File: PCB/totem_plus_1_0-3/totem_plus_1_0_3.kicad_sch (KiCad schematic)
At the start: 92 parts, among them J1 MJ-4PP-9, J2 MJ-4PP-9, U1 xiao-ble, U2 xiao-ble

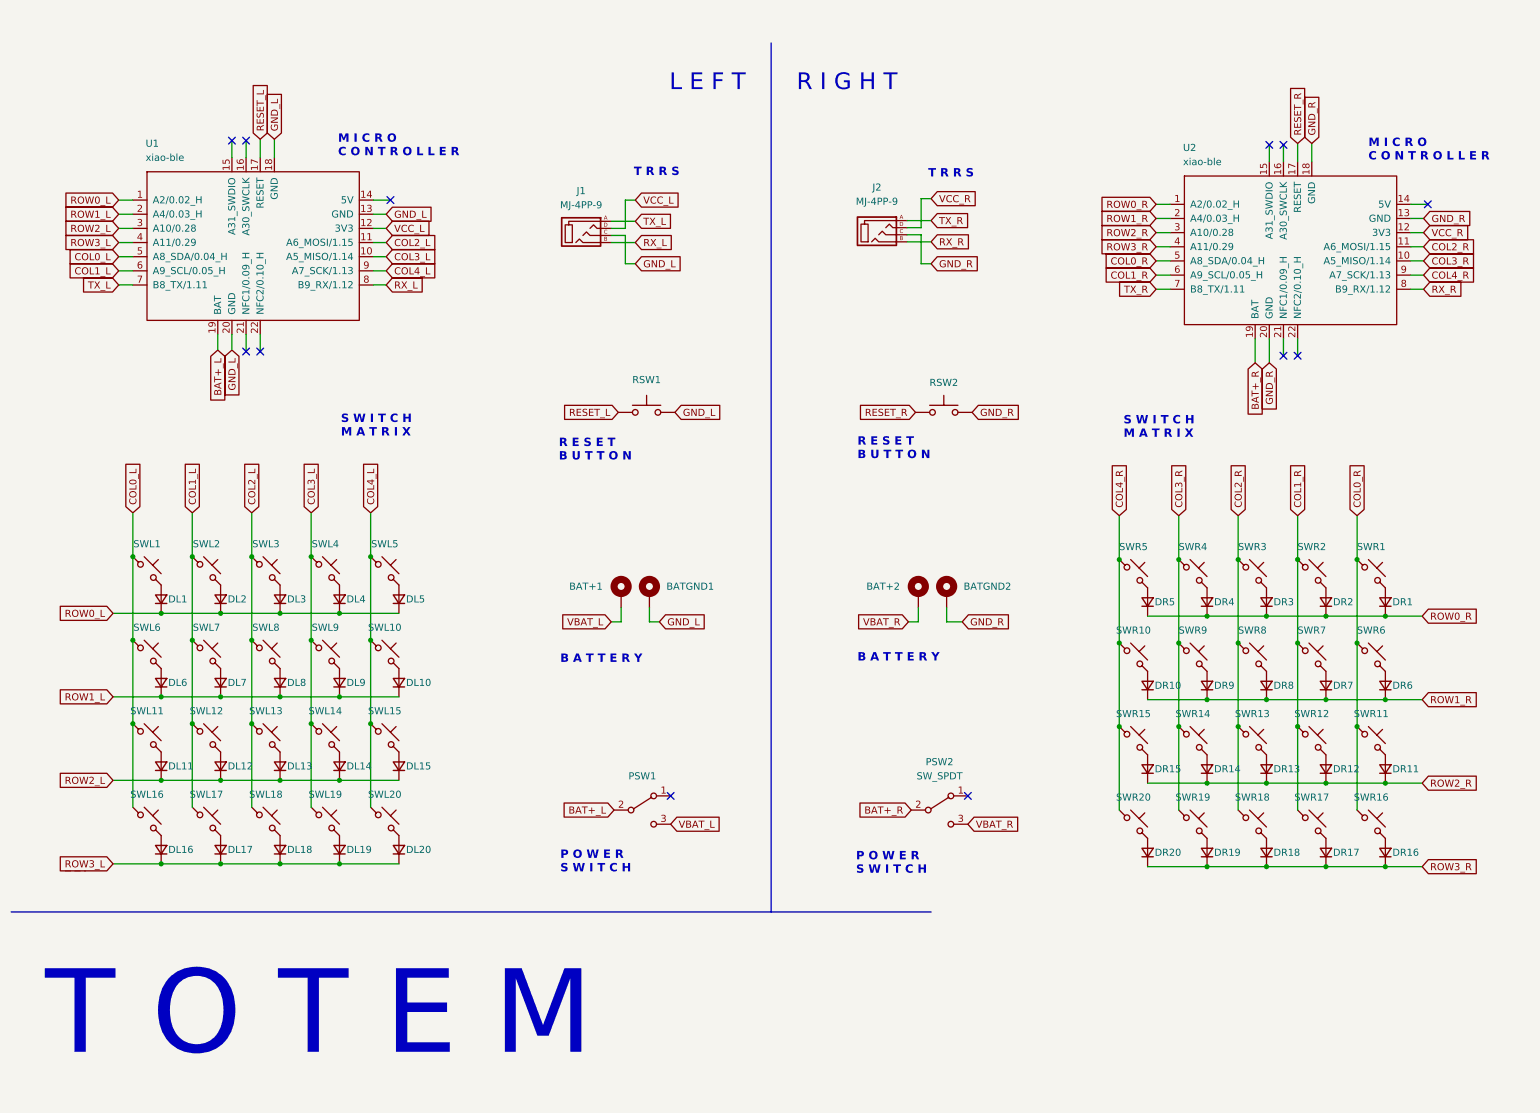
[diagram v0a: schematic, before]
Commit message: Added option to add a switch (like the power switch) instead of a TRRS jack as a 'key' - ie as a layer switch
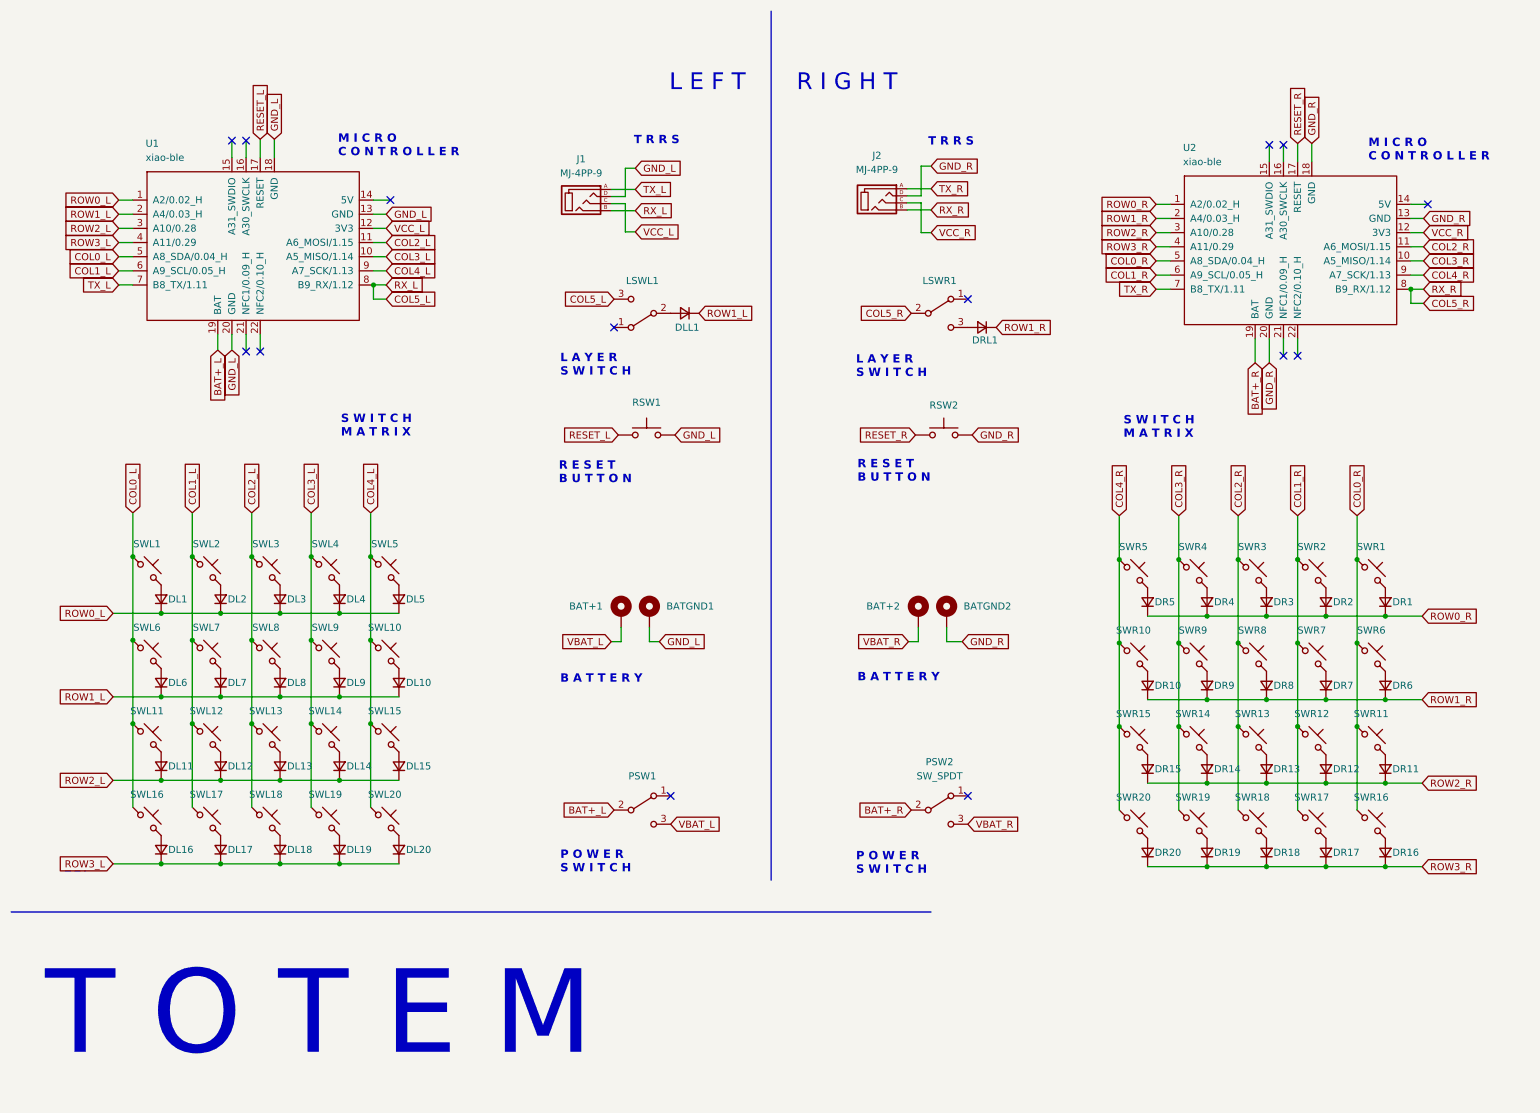
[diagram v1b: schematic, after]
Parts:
- added DLL1, DRL1: D_Small, TOTEMlib:Diode_SOD123, symbol Device:D_Small
- added LSWL1, LSWR1: SW_SPDT, TOTEMlib:MSK12C02, symbol Switch:SW_SPDT
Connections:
- net GND_L: now also J1.D; no longer J1.C
- net GND_R: now also J2.D; no longer J2.C
- net ROW1_L: now also DLL1.1 (K)
- net ROW1_R: now also DRL1.1 (K)
- net VCC_L: now also J1.C; no longer J1.D
- net VCC_R: now also J2.C; no longer J2.D
- net RX_L renamed COL5_L
- net COL5_L: now also LSWL1.3 (C)
- net RX_R renamed COL5_R
- net COL5_R: now also LSWR1.2 (B)
- new net: DRL1.2 (A), LSWR1.3 (C)
- new net: DLL1.2 (A), LSWL1.2 (B)
- no-connect marks 12 -> 14
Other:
- note added: "L A Y E R S W I T C H"
- moved on the sheet: BAT+1, BAT+2, BATGND1, BATGND2, J1, J2, RSW1, RSW2

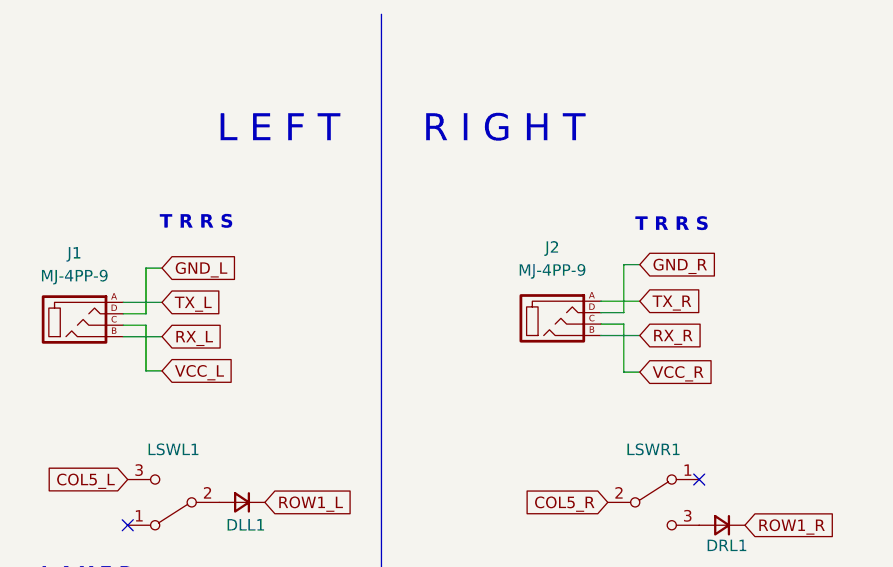
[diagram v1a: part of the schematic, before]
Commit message: updates PCB to remove the self-grounding error, and updates the README accordingly
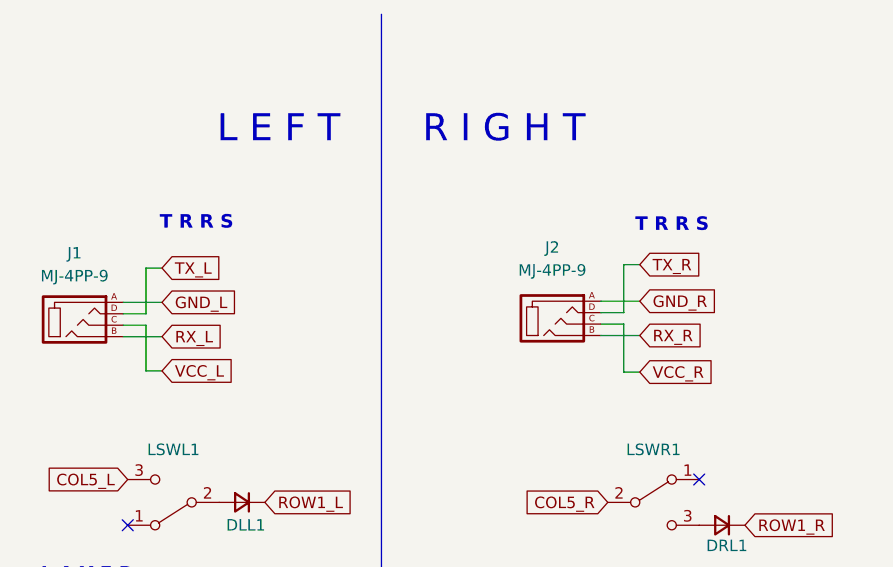
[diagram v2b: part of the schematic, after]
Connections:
- net GND_L: now also J1.A; no longer J1.D
- net GND_R: now also J2.A; no longer J2.D
- net TX_L: now also J1.D; no longer J1.A
- net TX_R: now also J2.D; no longer J2.A
